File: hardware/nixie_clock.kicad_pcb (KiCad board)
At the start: 2 copper layers, 224 x 70 mm, 84 parts, among them J1 Conn_02x02_Odd_Even, J2 USB_C_Receptacle_USB2.0_16P, J7 Barrel_Jack_Switch, Q1 IRF740, U1 AP63203WU, U2 MAX1771xSA, U3 ESP32-C3-WROOM-02, U4 HV5622PG, U5 HV5622PG

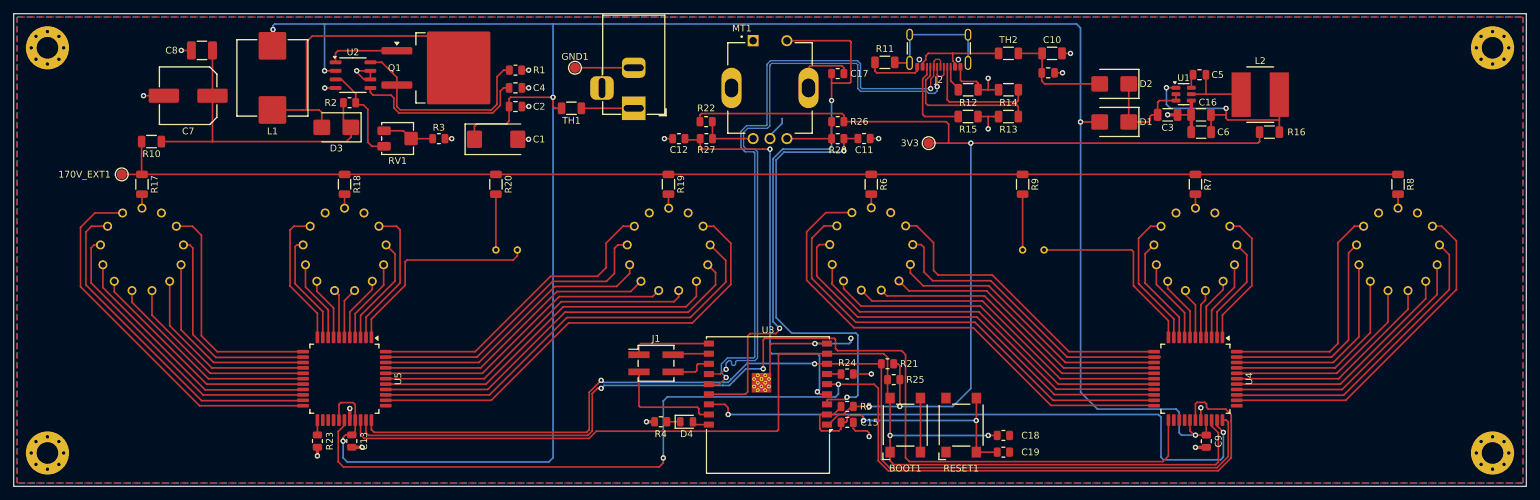
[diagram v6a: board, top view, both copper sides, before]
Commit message: Remap /LE and /BL to GPIO2 and GPIO1. SPI2 clk to GPIO6, SPI2 data to GPIO7.
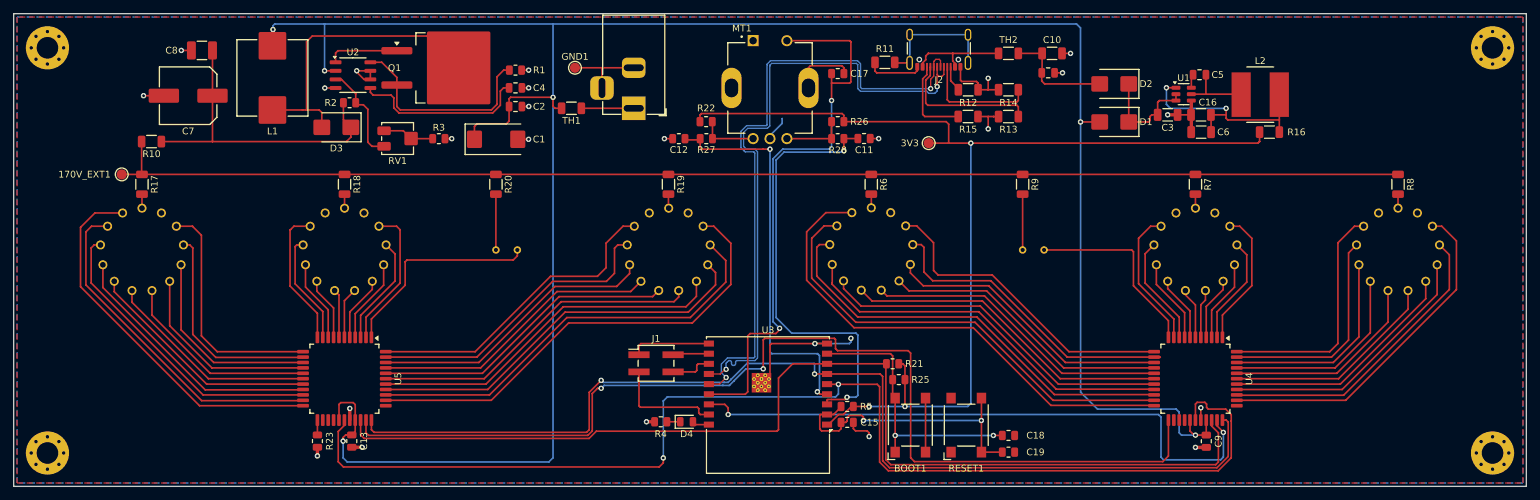
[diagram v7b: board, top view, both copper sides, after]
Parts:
- removed R24: 10k, Resistor_SMD:R_0805_2012Metric
- moved R25 0.75 mm to (181.1, 114.2)
- moved BOOT1 0.75 mm to (182.8, 120.9)
- moved C18 0.75 mm to (197.3, 122.5)
- moved C19 0.75 mm to (197.3, 124.9)
- moved R21 0.75 mm to (180.2, 111.8)
- moved RESET1 0.75 mm to (191.1, 120.9)
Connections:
- BOOT1 pad 1: /cpu/GPIO2 -> Net-(U3-IO9)
- C18 pad 1: /cpu/GPIO2 -> Net-(U3-IO9)
- R21 pad 2: /cpu/GPIO1 -> /cpu/GPIO2
- R25 pad 2: /cpu/GPIO2 -> Net-(U3-IO9)
- U3 pad 6: Net-(U3-IO7) -> /cpu/GPIO1
- U3 pad 7: /cpu/GPIO1 -> /cpu/GPIO2
- U3 pad 8: /cpu/GPIO2 -> Net-(U3-IO9)
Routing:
- net Net-(U3-IO9): track 0.00 -> 40.2 mm, vias 0 -> 2
- net /cpu/GPIO2: track 180.0 -> 160.7 mm, vias 2 -> 0
- net /connectors/GND: track 125.6 -> 122.9 mm, vias 26 -> 25
- net Net-(U3-IO7): track 2.07 -> 0.00 mm
- net /cpu/3.3V: track 159.3 -> 160.6 mm
- net Net-(U3-EN): track 42.7 -> 43.7 mm

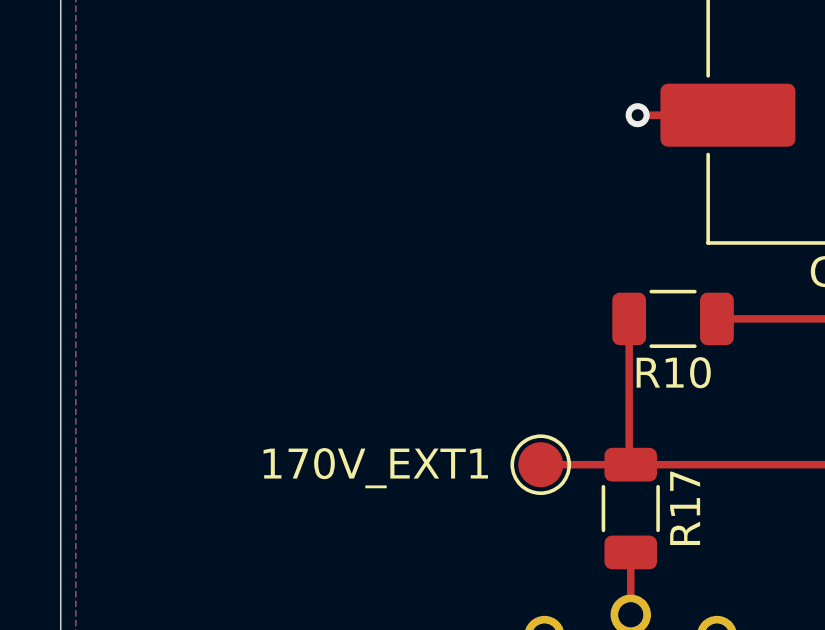
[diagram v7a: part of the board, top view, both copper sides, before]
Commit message: Add high voltage symbol.
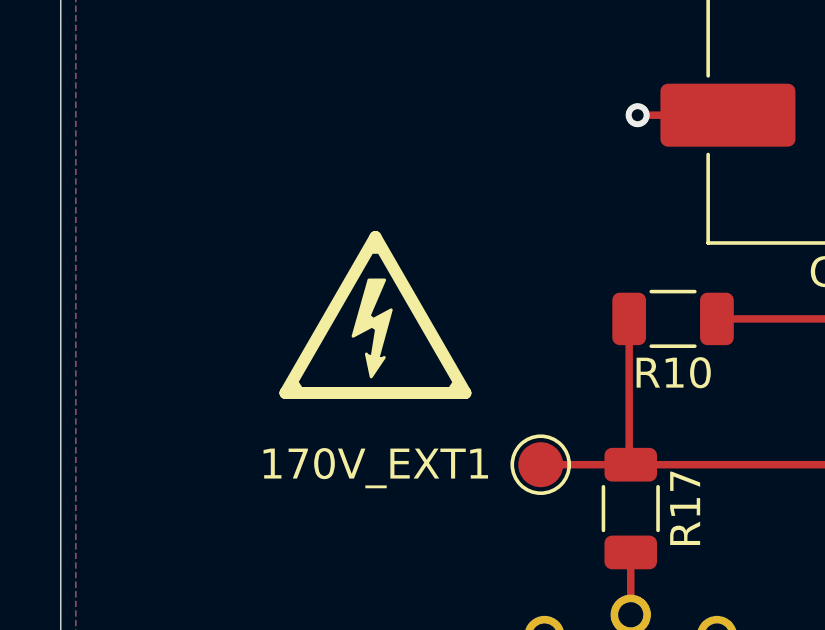
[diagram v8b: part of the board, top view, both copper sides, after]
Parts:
- added REF**: Symbol_HighVoltage_Triangle_6x6mm_Copper, Symbol:Symbol_HighVoltage_Triangle_6x6mm_Copper, F.Cu at (60.5, 78.8)
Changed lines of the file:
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@@
 		)
 	)
+	(footprint "Symbol:Symbol_HighVoltage_Triangle_6x6mm_Copper"
+		(layer "F.Cu")
+		(at 60.49 78.81)
+		(descr "High voltage symbol, in triangle, 6x6mm, copper layer")
+		(tags "warning graphic")
+		(property "Reference" "REF**"
+			(at 0 -3.5 0)
+			(layer "F.SilkS")
+			(hide yes)
+			(effects
+				(font
+					(size 1 1)
+					(thickness 0.15)
+				)
+			)
+		)
+		(property "Value" "Symbol_HighVoltage_Triangle_6x6mm_Copper"
+			(at 0 3.5 0)
+			(layer "F.SilkS")
+			(hide yes)
+			(effects
+				(font
+					(size 1 1)
+					(thickness 0.15)
+				)
+			)
+		)
+		(property "Datasheet" ""
+			(at 0 0 0)
+			(unlocked yes)
+			(layer "F.Fab")
+			(hide yes)
+			(effects
+				(font
+					(size 1.27 1.27)
+					(thickness 0.15)
+				)
+			)
+		)
+		(property "Description" ""
+			(at 0 0 0)
+			(unlocked yes)
+			(layer "F.Fab")
+			(hide yes)
+			(effects
+				(font
+					(size 1.27 1.27)
+					(thickness 0.15)
+				)
+			)
+		)
+		(attr board_only exclude_from_pos_files exclude_from_bom)
+		(fp_line
+			(start -3 2.6)
+			(end 0 -2.6)
+			(stroke
+				(width 0.4)
+				(type solid)
+			)
+			(layer "F.SilkS")
+		)
+		(fp_line
+			(start -2.456839 2.564632)
+			(end -2.723161 2.155368)
+			(stroke
+				(width 0.2)
+				(type solid)
+			)
+			(layer "F.SilkS")
+		)
+		(fp_line
+			(start -0.28 0.03)
+			(end -0.08 0.21)
+			(stroke
+				(width 0.2)
+				(type solid)
+			)
+			(layer "F.SilkS")
+		)
+		(fp_line
+			(start -0.26 1.36)
+			(end 0.21 1.46)
+			(stroke
+				(width 0.1016)
+				(type solid)
+			)
+			(layer "F.SilkS")
+		)
+		(fp_line
+			(start -0.135 0.295)
+			(end 0.115 0.465)
+			(stroke
+				(width 0.2)
+				(type solid)
+			)
+			(layer "F.SilkS")
+		)
+		(fp_line
+			(start -0.125 -2.14)
+			(end 0.125 -2.14)
+			(stroke
+				(width 0.2)
+				(type solid)
+			)
+			(layer "F.SilkS")
+		)
+		(fp_line
+			(start 0 -2.6)
+			(end 3 2.6)
+			(stroke
+				(width 0.4)
+				(type solid)
+			)
+			(layer "F.SilkS")
+		)
+		(fp_line
+			(start 2.466839 2.564632)
+			(end 2.733161 2.155368)
+			(stroke
+				(width 0.2)
+				(type solid)
+			)
+			(layer "F.SilkS")
+		)
+		(fp_line
+			(start 3 2.6)
+			(end -3 2.6)
+			(stroke
+				(width 0.4)
+				(type solid)
+			)
+			(layer "F.SilkS")
+		)
+		(fp_poly
+			(pts
+				(xy -0.321167 0.284) (xy 0.5255 -0.171083) (xy 0.04925 1.564583) (xy 0.292667 1.416417) (xy -0.14125 2.062)
+				(xy -0.3 1.3) (xy -0.130667 1.532834) (xy 0.070417 0.273417) (xy -0.7445 0.707334) (xy -0.215334 -1.165916)
+				(xy 0.30325 -1.165916)
+			)
+			(stroke
+				(width 0.1)
+				(type solid)
+			)
+			(fill yes)
+			(layer "F.SilkS")
+		)
+		(embedded_fonts no)
+	)
 	(footprint "Resistor_SMD:R_0805_2012Metric"
 		(layer "F.Cu")
@@
 		(min_thickness 0.25)
 		(filled_areas_thickness no)
-		(fill yes
+		(fill
 			(thermal_gap 0.5)
 			(thermal_bridge_width 0.5)
@@
 		(min_thickness 0.25)
 		(filled_areas_thickness no)
-		(fill yes
+		(fill
 			(thermal_gap 0.5)
 			(thermal_bridge_width 0.5)
